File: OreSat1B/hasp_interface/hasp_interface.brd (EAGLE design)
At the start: 83 x 100 mm, 79 parts, among them J1 SAMTEC-MMS-104-02-X-SHJ, J2 ORESAT-DEBUG-CONNECTOR-ALL, Q1 MMBT2907SMD, U1 TCAN330, U10 TPS63070, U2 LM60440ARPKR, U7 STM32F091C, X1 16MHZ-2.5x2mm

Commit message: Wire cleanup
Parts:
- removed DB9: (no value), con-lstb:MA09-1
- removed EDAC: (no value), con-lstb:MA12-2
- added J3: MEC2-40-01-X-DV-WT, MEC2-40-01-X-DV-WT:SAMTEC_MEC2-40-01-X-DV-WT
- added J5: TW-09-03-G-S-245-145, TW-09-03-G-S-245-145:SAMTEC_TW-09-03-G-S-245-145
- moved C6 160.1 mm to (37.9, 81.3), turned to 90 degrees
- moved D2 156.5 mm to (40.3, 72.9), turned to 270 degrees
- moved C5 156.3 mm to (36.5, 81.3), turned to 90 degrees
- moved C4 152.4 mm to (35.0, 81.3), turned to 90 degrees
- moved C3 138.1 mm to (33.6, 81.3), turned to 90 degrees
- moved L2 137.6 mm to (41.0, 79.5), turned to 90 degrees
- moved C2 127.4 mm to (36.2, 72.9), turned to 270 degrees
- moved D1 125.8 mm to (42.0, 73.0), flipped to the bottom
- moved C1 125.2 mm to (49.1, 77.3), turned to 90 degrees
- moved R7 125.1 mm to (46.1, 75.0), turned to 180 degrees
- moved Q1 120.8 mm to (45.9, 77.5), turned to 90 degrees
- moved R5 110.5 mm to (32.9, 72.9), turned to 90 degrees
- moved R4 107.5 mm to (34.6, 72.9), turned to 270 degrees
- moved R3 105.3 mm to (37.9, 72.9), turned to 90 degrees
- moved U2 91.7 mm to (35.1, 77.7)
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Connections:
- net +30VDC: now also J3.01, J3.02, J3.03, J3.04; no longer EDAC.1, EDAC.2, EDAC.3, EDAC.4
- net GND: now also J3.12, J3.18, J3.20, J3.21, J3.23; no longer EDAC.12, EDAC.18, EDAC.20, EDAC.21, EDAC.23
- net TURNSTILEFIRE-(DISCRETE1): now also J3.06; no longer EDAC.6
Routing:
- net 3.3V: track 259.1 -> 217.9 mm, vias 17 -> 14
- net N$7: track 0.00 -> 40.7 mm, vias 0 -> 3
- net TURNSTILEFIRE-(DISCRETE1): track 0.00 -> 38.2 mm, vias 0 -> 2
- net N$2: track 0.00 -> 19.9 mm, vias 0 -> 3
- net TPS-VIN: track 3.38 -> 23.2 mm
- net !SHUTDOWN: track 72.6 -> 91.0 mm, vias 2 -> 3
- net GND: track 21.1 -> 39.2 mm, vias 1197 -> 653
- net +30VDC: track 0.00 -> 12.6 mm, vias 0 -> 1
- net N$4: track 0.00 -> 11.3 mm, vias 0 -> 1
- net VBUS: track 18.3 -> 28.4 mm
- net N$6: track 0.00 -> 9.93 mm, vias 0 -> 2
- net N$8: track 0.00 -> 7.75 mm
- net N$1: track 27.2 -> 20.6 mm
- net N$5: track 0.00 -> 6.25 mm, vias 0 -> 2
- removed copper zone on layer 1, net VSOLAR

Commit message: Updated schematic
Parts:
- added R8: 10k, oresat-rcl:.0603-C-NOSILK
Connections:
- removed net LT1618-ENABLE: U7.11
- removed net LT1618-IADJ: U7.14
- new net N$9: D2.A, R8.1
- net N$8: now also R8.2; no longer D2.A
- net TURNSTILEFIRE-(DISCRETE1): no longer J3.06
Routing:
- net LT1618-IADJ: track 29.3 -> 0.00 mm, vias 1 -> 0
- net LT1618-ENABLE: track 28.8 -> 0.00 mm, vias 1 -> 0
- net N$8: track 7.75 -> 7.15 mm
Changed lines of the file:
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@@
 <attribute name="VALUE" x="52.3" y="59.7" size="1.27" layer="27" rot="R180"/>
+</element>
+<element name="R8" library="oresat-rcl" package=".0603-C-NOSILK" value="10k" x="0.5" y="-14.1" smashed="yes">
+<attribute name="NAME" x="-0.5" y="-13.35" size="0.5" layer="25" font="vector" ratio="15"/>
+<attribute name="NAME" x="0.5" y="-14.1" size="0.3" layer="33" ratio="15" align="center"/>
+<attribute name="VALUE" x="-0.5" y="-15.65" size="0.8" layer="27" font="vector" ratio="15"/>
 </element>
 </elements>
@@
 <wire x1="16.8" y1="76.7" x2="14.8" y2="76.7" width="0.3048" layer="1"/>
 </signal>
-<signal name="LT1618-ENABLE">
-<contactref element="U7" pad="11"/>
-<wire x1="72.5037" y1="84.05" x2="71.6" y2="83.1463" width="0.2" layer="1"/>
-<wire x1="74.15" y1="84.05" x2="72.5037" y2="84.05" width="0.2" layer="1"/>
-<wire x1="56.2" y1="81.5" x2="49.5" y2="74.8" width="0.2" layer="16"/>
-<wire x1="70.5" y1="81.5" x2="71.6" y2="82.6" width="0.2" layer="16"/>
-<wire x1="56.2" y1="81.5" x2="70.5" y2="81.5" width="0.2" layer="16"/>
-<via x="71.6" y="82.6" extent="1-16" drill="0.254"/>
-<wire x1="71.6" y1="82.6" x2="71.6" y2="83.1463" width="0.2" layer="1"/>
-</signal>
 <signal name="TPS-VAUX">
 <contactref element="U10" pad="6"/>
@@
 </polygon>
 </signal>
-<signal name="LT1618-IADJ">
-<contactref element="U7" pad="14"/>
-<wire x1="72.15" y1="86.05" x2="72.15" y2="85.191425" width="0.2" layer="1"/>
-<wire x1="67.858575" y1="80.9" x2="67" y2="80.9" width="0.2" layer="1"/>
-<wire x1="72.15" y1="85.191425" x2="67.858575" y2="80.9" width="0.2" layer="1"/>
-<wire x1="48.7" y1="73.2" x2="56.4" y2="80.9" width="0.2" layer="16"/>
-<via x="67" y="80.9" extent="1-16" drill="0.254"/>
-<wire x1="67" y1="80.9" x2="56.4" y2="80.9" width="0.2" layer="16"/>
-</signal>
 <signal name="XTAL1-IN">
 <contactref element="C28" pad="1"/>
@@
 <wire x1="40" y1="72.5" x2="40" y2="72.6" width="0.2" layer="16"/>
 <wire x1="67.1" y1="74.6" x2="64.2" y2="71.7" width="0.2" layer="16"/>
-<contactref element="J3" pad="06"/>
-<wire x1="8.5" y1="-5" x2="40.1524" y2="72.4476" width="0" layer="19" extent="1-16"/>
 </signal>
 <signal name="N$2">
@@
 <signal name="N$8">
 <contactref element="U2" pad="9"/>
-<contactref element="D2" pad="A"/>
 <wire x1="39.6" y1="73.5" x2="39.7" y2="73.4" width="0.2" layer="1"/>
-<wire x1="39.7" y1="73.4" x2="40.3" y2="73.4" width="0.2" layer="1"/>
 <wire x1="35.9763" y1="77.7" x2="38.2" y2="77.7" width="0.2" layer="1"/>
 <wire x1="38.2" y1="77.7" x2="39.6" y2="76.3" width="0.2" layer="1"/>
 <wire x1="39.6" y1="76.3" x2="39.6" y2="73.5" width="0.2" layer="1"/>
+<contactref element="R8" pad="2"/>
+<wire x1="1.2" y1="-14.1" x2="39.7" y2="73.4" width="0" layer="19" extent="1-1"/>
+</signal>
+<signal name="N$9">
+<contactref element="R8" pad="1"/>
+<contactref element="D2" pad="A"/>
+<wire x1="-0.2" y1="-14.1" x2="40.3" y2="73.4" width="0" layer="19" extent="1-1"/>
 </signal>
 </signals>

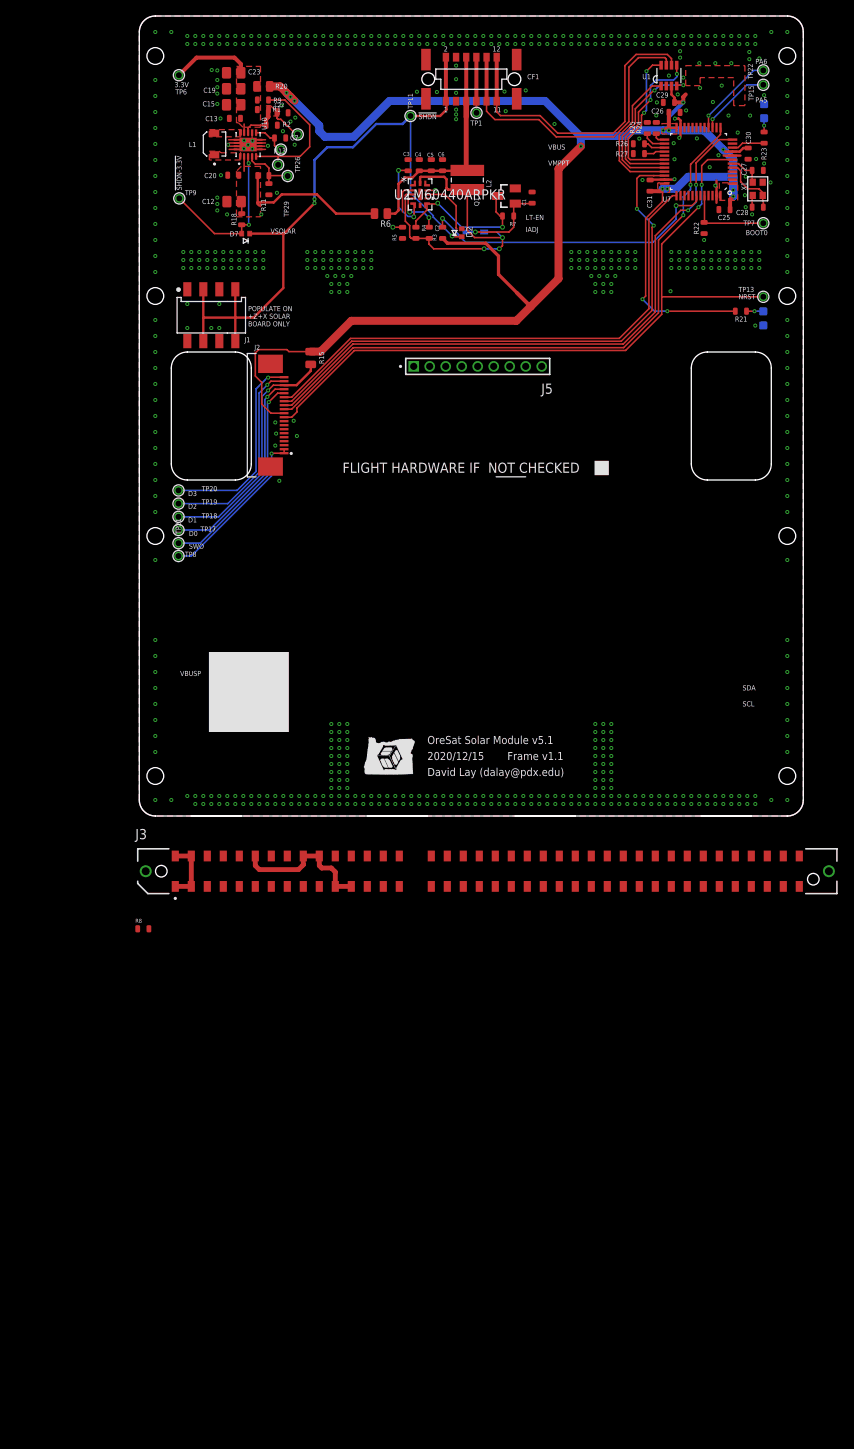
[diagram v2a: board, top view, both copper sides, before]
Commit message: Cleaned up and fixed errors on 30V SPS, removed some old solar module cruft.
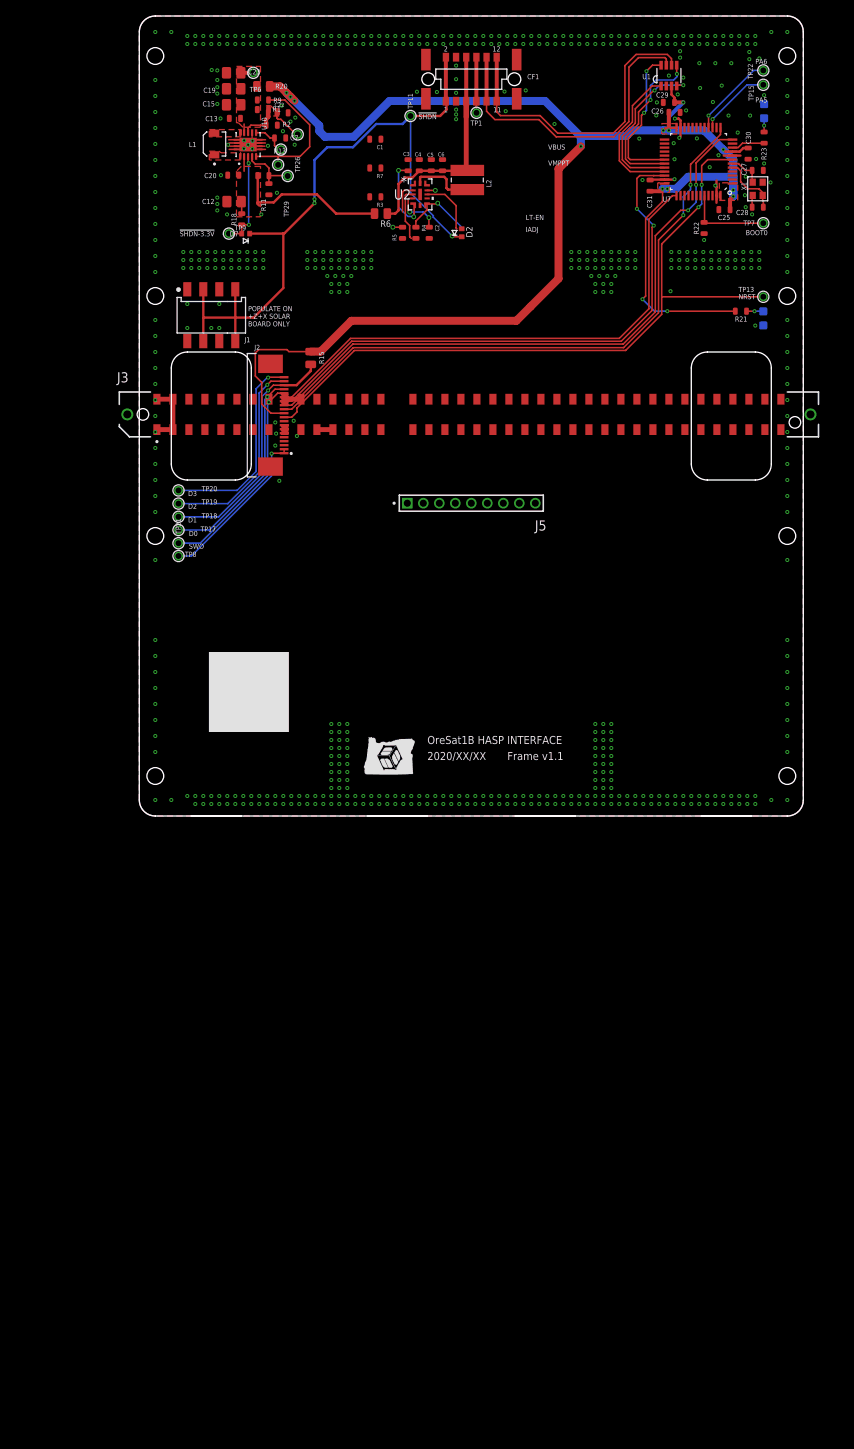
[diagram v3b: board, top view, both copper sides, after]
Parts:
- removed D1: CMDD6001, D-Central-CMDD6001-silicon-low-leakage:SOD323
- removed Q1: MMBT2907SMD, Q-Diodesinc-MMBT2907-PNP:SOT23-BEC
- removed R24, R25, R26, R27: 1k/NP, oresat-rcl:.0603-C-NOSILK
- removed R8: 10k, oresat-rcl:.0603-C-NOSILK
- removed U$1: FLIGHMARKERNEW, oresat-flight-marker:FLIGHTMARKER_NEW_BOARDS
- C1: value TBD -> 10u / 75V
- R7: value TBD -> 1k
- moved J3 57.1 mm to (41.2, 50.2)
- moved C1 20.9 mm to (29.5, 84.6), turned to 180 degrees
- moved R7 17.7 mm to (29.5, 81.0)
- moved J5 17.1 mm to (33.5, 39.1)
- moved R3 9.54 mm to (29.5, 77.4), turned to 180 degrees
- moved TP6 9.30 mm to (14.2, 92.9)
- moved TP9 7.60 mm to (11.2, 72.8)
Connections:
- removed net N$4: C1.1, D1.2, Q1.B, R7.1
- removed net N$8: R8.2, U2.9
- removed net SMSN0: R24.1, U7.25
- removed net SMSN1: R25.1, U7.26
- removed net SMSN2: R26.1, U7.27
- removed net SMSN3: R27.1, U7.28
- removed net TURNSTILEFIRE-(DISCRETE1): R3.2, U7.42
- net +30VDC: now also C1.1, R3.1
- net 3.3V: no longer R3.1
- net GND: now also J3.17, R7.2; no longer Q1.E, R24.2, R25.2, R26.2, R27.2
- net N$2: no longer Q1.C, R7.2
- net N$7: no longer D1.1, R4.2
- net N$9: now also R3.2, R7.1, U2.9; no longer R8.1
- net VBUS: now also R4.2
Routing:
- net TURNSTILEFIRE-(DISCRETE1): track 38.2 -> 0.00 mm, vias 2 -> 0
- net N$7: track 40.7 -> 14.7 mm, vias 3 -> 0
- net 3.3V: track 217.9 -> 200.9 mm
- net GND: track 39.2 -> 25.1 mm
- net N$4: track 11.3 -> 0.00 mm, vias 1 -> 0
- net N$2: track 19.9 -> 10.3 mm, vias 3 -> 2
- net TPS-VOUT-3.3V: track 11.2 -> 2.64 mm
- net !SHDN-3.3V: track 20.2 -> 12.2 mm
- net N$9: track 0.00 -> 7.15 mm
- net N$8: track 7.15 -> 0.00 mm
- net SMSN1: track 3.00 -> 0.00 mm
- net SMSN2: track 2.70 -> 0.00 mm
- net SMSN3: track 2.60 -> 0.00 mm
- net SMSN0: track 1.64 -> 0.00 mm
- removed copper zone on layer 1, net N$3
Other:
- board text added: "2020/XX/XX"
- board text added: "OreSat1B HASP INTERFACE"
- board text removed: "David Lay (dalay@pdx.edu)"
- board text removed: "SCL"
- board text removed: "SDA"
- board text removed: "VBUSP"
- board text removed: "VSOLAR"

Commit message: Added new cots dc dc converter and updated HASP interface connection.
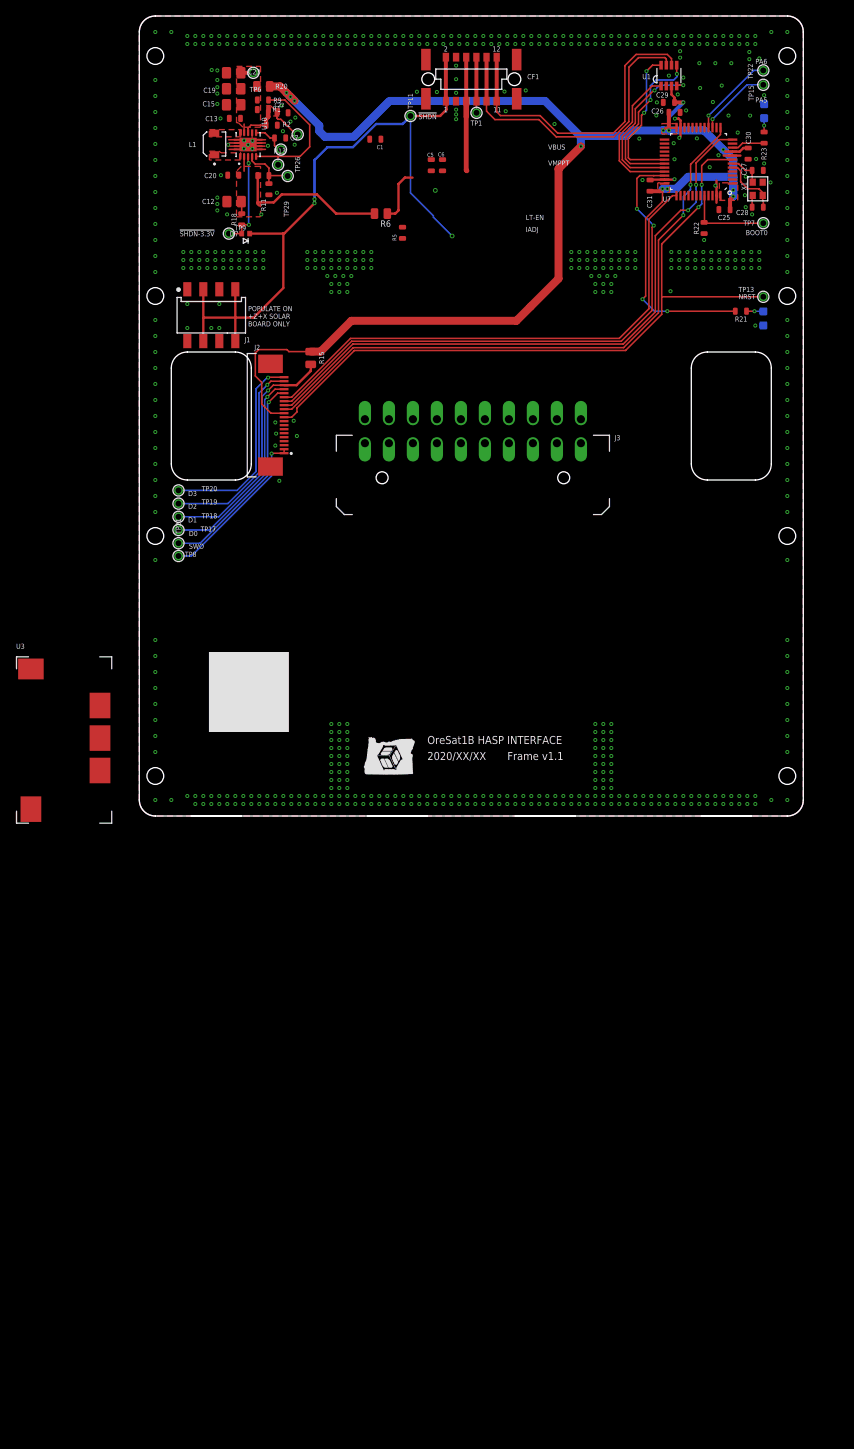
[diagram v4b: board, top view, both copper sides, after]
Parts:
- removed C2: 100n, oresat-rcl:.0603-C-NOSILK
- removed C3, R4: TBD, oresat-rcl:.0603-C-NOSILK
- removed C4: 10u, oresat-rcl:.0603-C-NOSILK
- removed D2: 1N4448HLP-7, D-0402-package:.0402-B-NOSILK-DIODE
- removed J5: TW-09-03-G-S-245-145, TW-09-03-G-S-245-145:SAMTEC_TW-09-03-G-S-245-145
- removed L2: L-BOURNS-SRN4018TA, L-Bourns-SRN4018TA:L-BOURNS-SRN4018TA
- removed R3: 10k, oresat-rcl:.0603-C-NOSILK
- removed R7: 1k, oresat-rcl:.0603-C-NOSILK
- removed U2: LM60440ARPKR, U-TI-LM6044DRPKR-buck:WQFN-HR-13_RPK_TEX
- added U3: OKI-T/36W-W40, U-Murata-OKI-T36-W40-DC-DC-Converter:OKI-T/36W-W40
- C5: value 10u -> NP
- J3: value MEC2-40-01-X-DV-WT -> MOLEX-43045XXXX; device MEC2-40-01-X-DV-WT:SAMTEC_MEC2-40-01-X-DV-WT -> J-Molex-043045XXXX-Dual-Row-Connector:0430452000
- R5: value TBD -> 3.8k
- moved J3 2.16 mm to (41.7, 48.1)
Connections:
- removed net N$5: C2.1, U2.4
- removed net N$6: C3.1, U2.5
- removed net N$7: C2.2, L2.1, U2.12, U2.3
- removed net N$9: D2.A, R3.2, R7.1, U2.9
- new net HASP_ANALOG_1: J3.4
- new net HASP_ANALOG_2: J3.3
- new net HASP_DISCRETE_1: J3.16
- new net HASP_DISCRETE_2: J3.15
- new net HASP_DISCRETE_3: J3.14
- new net HASP_DISCRETE_4: J3.13
- new net HASP_SERIAL_RX: J3.20
- new net HASP_SERIAL_TX: J3.10
- net !SHUTDOWN: no longer D2.C
- net +30VDC: now also J3.1, J3.11, J3.12, J3.2, U3.2; no longer J3.01, J3.02, J3.03, J3.04, R3.1, U2.10, U2.2
- net GND: now also J3.5, J3.6, J3.7, J3.8, J3.9, U3.1, U3.3; no longer C3.2, C4.2, J3.12, J3.20, J3.21, J3.23, R7.2, U2.1, U2.11, U2.6
- net N$2: now also U3.4; no longer R4.1, U2.7
- net VBUS: now also U3.5; no longer C4.1, L2.2, R4.2
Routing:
- net N$7: track 14.7 -> 0.00 mm
- net +30VDC: track 12.6 -> 0.00 mm
- net N$2: track 10.3 -> 0.00 mm, vias 2 -> 0
- net N$6: track 9.93 -> 0.00 mm, vias 2 -> 0
- net VBUS: track 28.4 -> 21.2 mm
- net N$9: track 7.15 -> 0.00 mm
- net N$5: track 6.25 -> 0.00 mm, vias 2 -> 0
- net GND: track 25.1 -> 21.1 mm
- net !SHUTDOWN: track 91.0 -> 89.9 mm

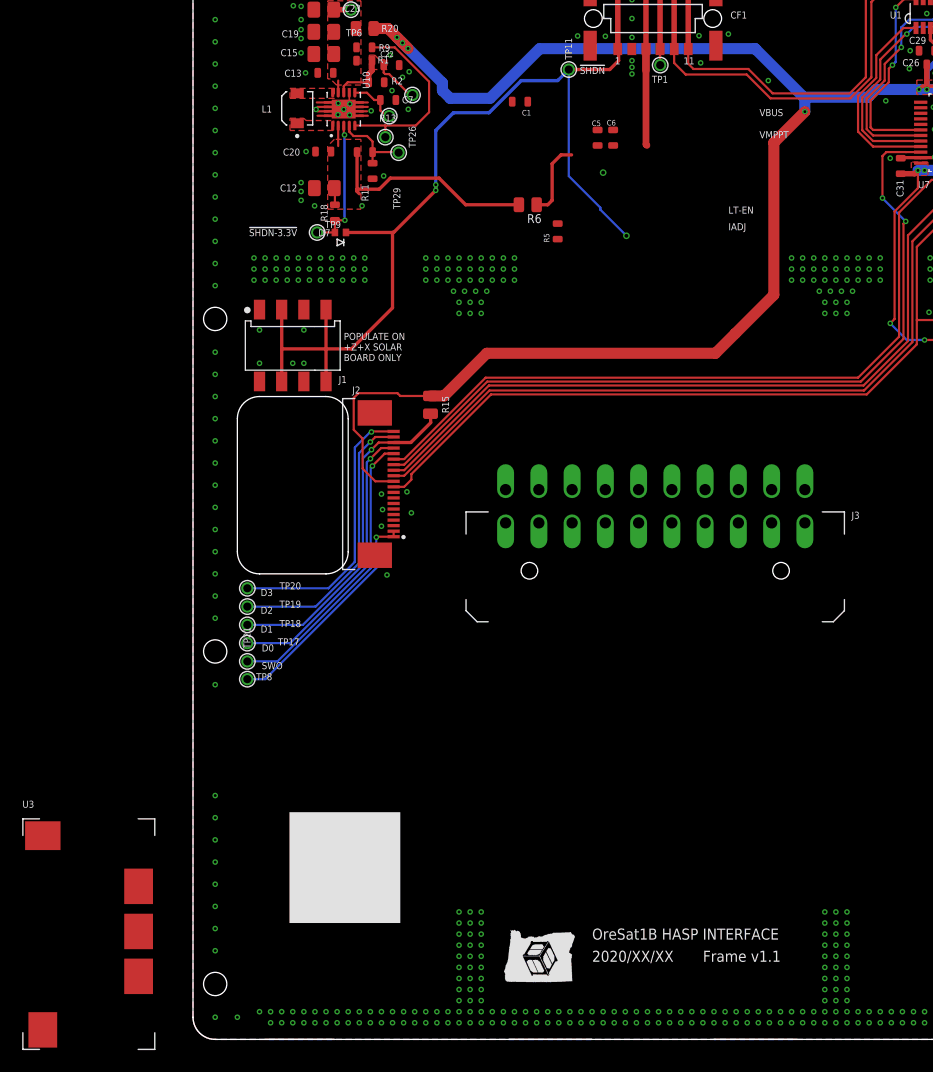
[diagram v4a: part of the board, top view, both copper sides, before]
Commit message: Updated connector footprint and did layout
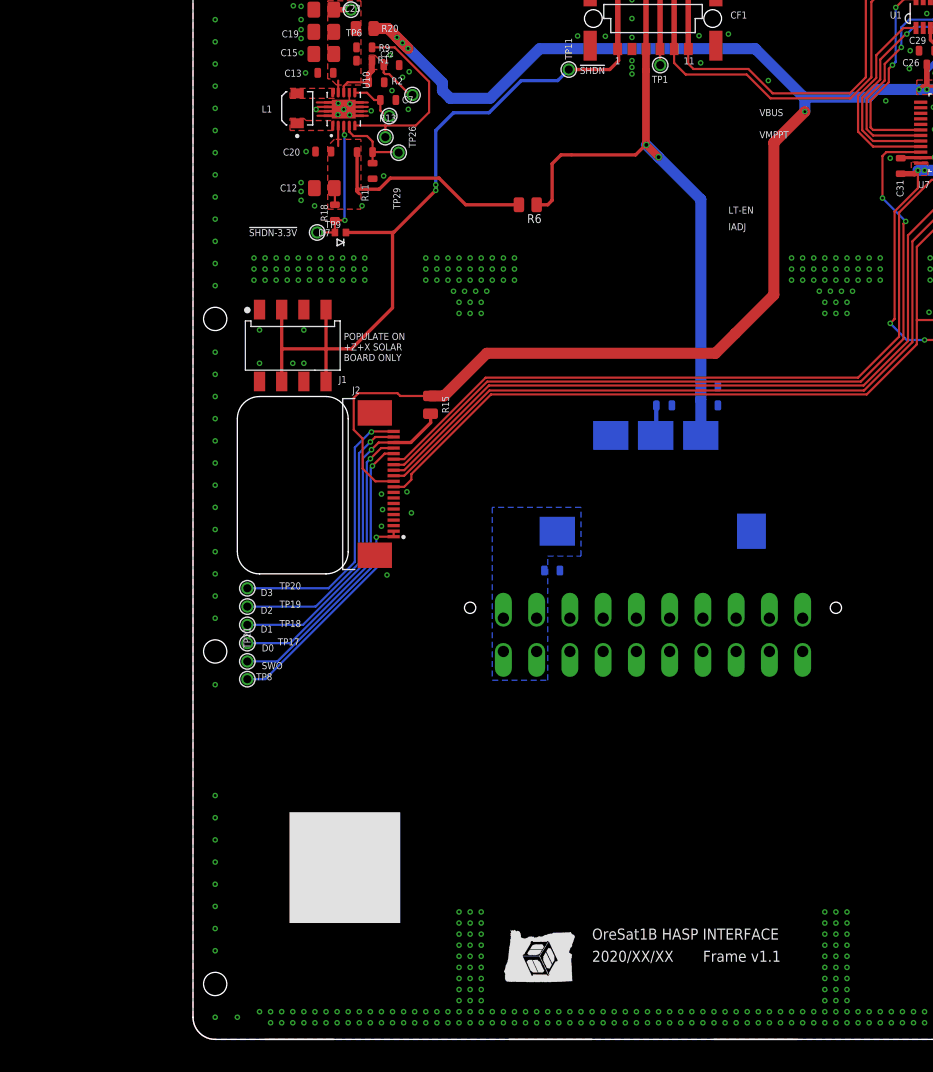
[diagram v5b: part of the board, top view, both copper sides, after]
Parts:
- J3: value MOLEX-43045XXXX -> MOLEX-43045XXXXVERTICAL; device J-Molex-043045XXXX-Dual-Row-Connector:0430452000 -> J-Molex-043045XXXX-Dual-Row-Connector:0430452012
- moved U3 65.0 mm to (41.5, 50.0), flipped to the bottom, turned to 90 degrees
- moved C1 42.4 mm to (32.4, 42.3), flipped to the bottom
- moved C5 26.2 mm to (46.6, 57.2), flipped to the bottom, turned to 180 degrees
- moved C6 24.1 mm to (46.6, 58.9), flipped to the bottom, turned to 180 degrees
- moved R5 18.4 mm to (42.5, 57.2), flipped to the bottom, turned to 0 degrees
- moved J3 11.6 mm to (41.5, 36.5), flipped to the bottom
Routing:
- net VBUS: track 21.2 -> 59.3 mm, vias 0 -> 2
- net !SHUTDOWN: track 89.9 -> 72.6 mm, vias 3 -> 2
- net N$2: track 0.00 -> 2.73 mm
- added copper zone on layer 16, net +30VDC
